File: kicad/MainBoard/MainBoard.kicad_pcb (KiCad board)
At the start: 2 copper layers, 191.5 x 166.3 mm, 99 parts, among them J1 CHAN1, J10 ACC Port, J11 433TX, J12 VDC INPUT, J13 BAT, J14 TRG1, J15 TRG2, J16 FP-BUTTONS, J17 EXPAN2, J18 OUTPUT_BOARD_POWER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

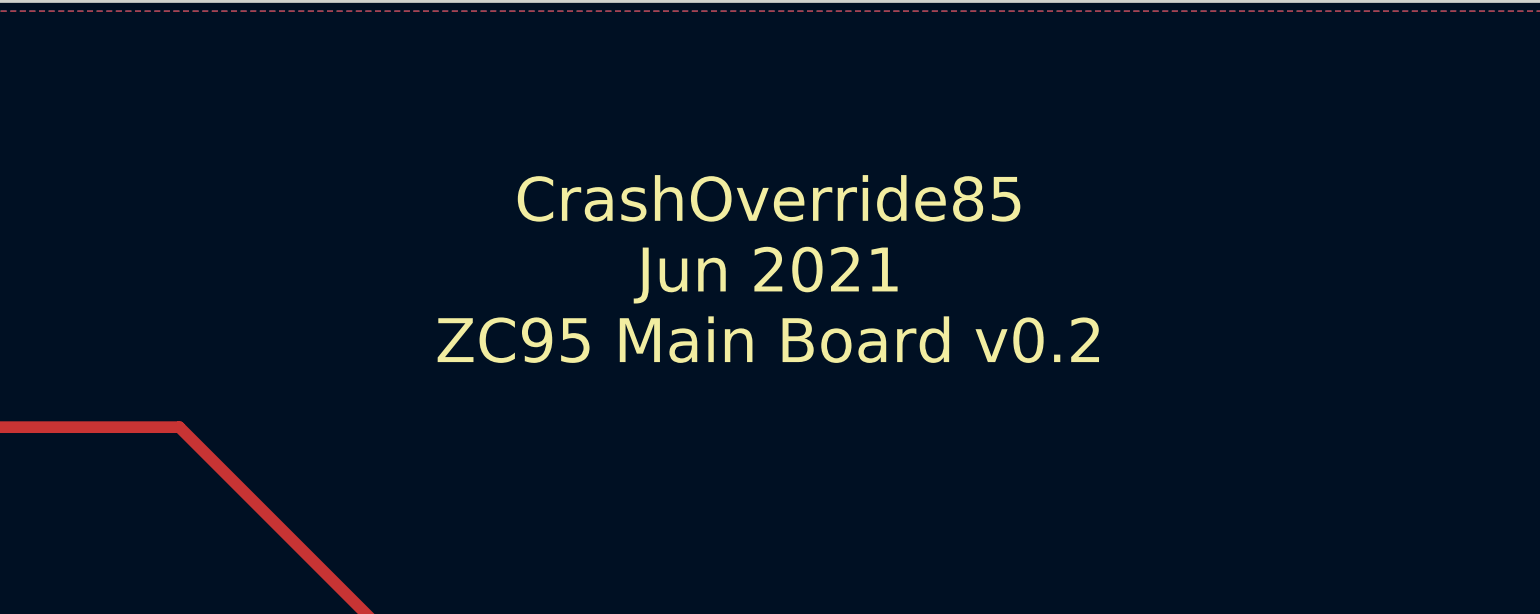
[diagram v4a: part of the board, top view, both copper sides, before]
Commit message: Move to fit new 3.5mm holes
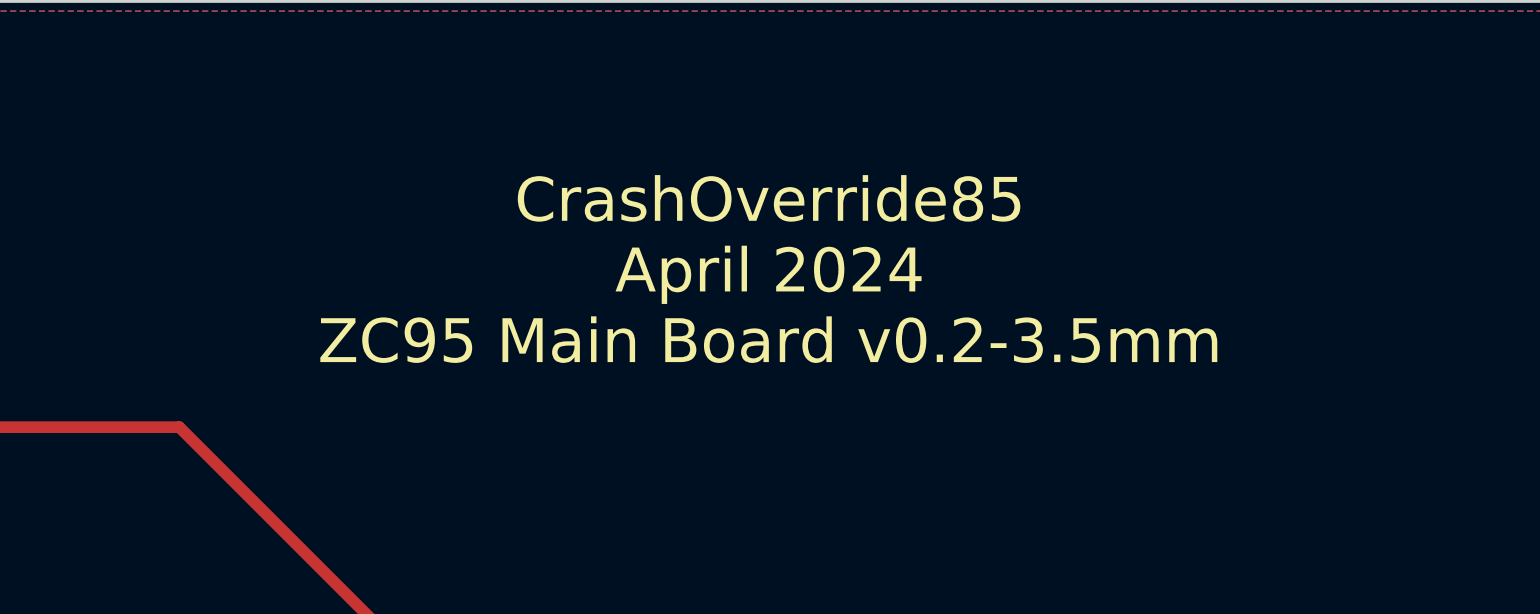
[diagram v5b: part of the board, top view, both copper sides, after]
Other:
- board text added: "CrashOverride85 April 2024 ZC95 Main Board v0.2-3.5mm"
- board text removed: "CrashOverride85 Jun 2021 ZC95 Main Board v0.2"
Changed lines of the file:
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@@
 		)
 	)
-	(gr_text "CrashOverride85\nJun 2021\nZC95 Main Board v0.2"
+	(gr_text "CrashOverride85\nApril 2024\nZC95 Main Board v0.2-3.5mm"
 		(at 170.815 25.4 0)
 		(layer "F.SilkS")

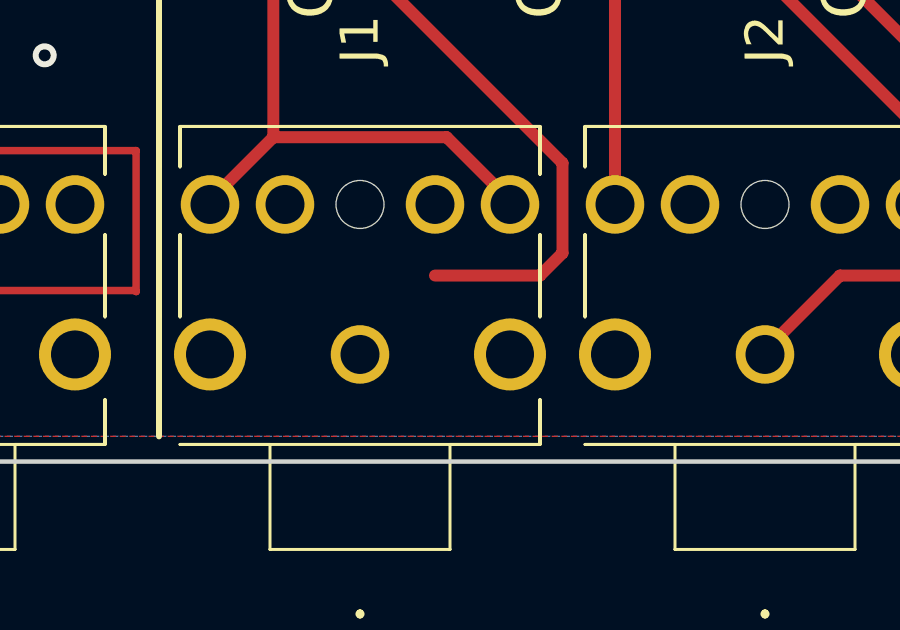
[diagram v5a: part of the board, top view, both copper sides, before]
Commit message: Fix missing connection on mainboard
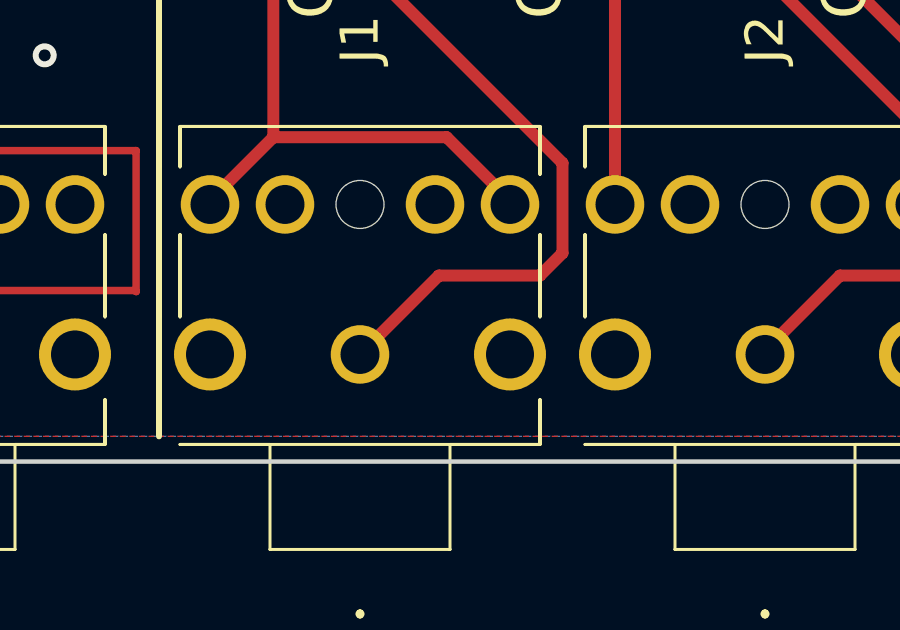
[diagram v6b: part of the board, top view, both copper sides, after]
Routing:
- net Net-(J4-Pin_2): track 25.5 -> 29.1 mm
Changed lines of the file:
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@@
+	)
+	(segment
+		(start 158.75 176.25)
+		(end 155.38 176.25)
+		(width 0.4)
+		(layer "F.Cu")
+		(net 13)
 	)
 	(segment
@@
 	)
 	(segment
-		(start 155.25 176.25)
-		(end 158.75 176.25)
+		(start 155.38 176.25)
+		(end 152.75 178.88)
 		(width 0.4)
 		(layer "F.Cu")
